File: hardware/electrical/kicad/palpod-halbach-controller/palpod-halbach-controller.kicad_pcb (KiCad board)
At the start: 4 copper layers, 150 x 100 mm, 0 parts

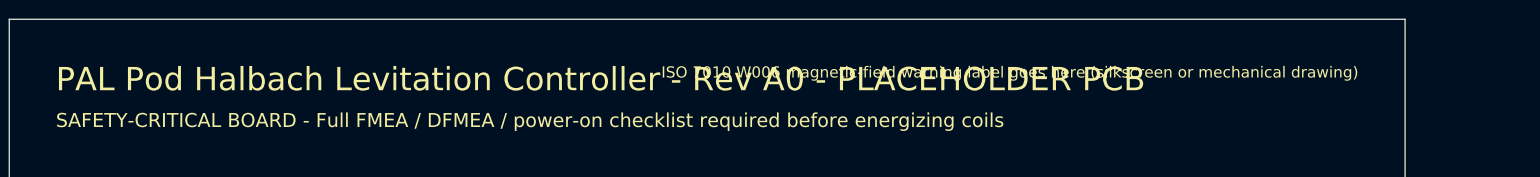
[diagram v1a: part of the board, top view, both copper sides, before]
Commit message: brand: broad KiCad sweep — remaining PAL Pod strings → Hearth
Targeted-pattern sed in ff14a48 missed variants. Broad find-replace
on .kicad_sch/pcb/pro/sym/mod + fp-lib-table + sym-lib-table +
per-project README.md (only where PAL Pod string actually appeared).
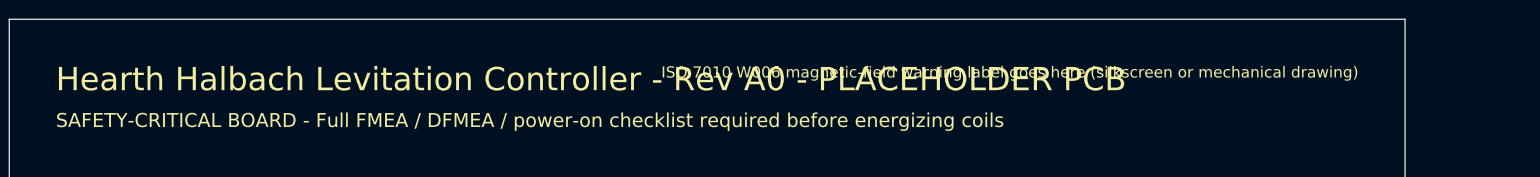
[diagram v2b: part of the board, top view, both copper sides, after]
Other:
- board text added: "Hearth Halbach Levitation Controller - Rev A0 - PLACEHOLDER PCB"
- board text removed: "PAL Pod Halbach Levitation Controller - Rev A0 - PLACEHOLDER PCB"
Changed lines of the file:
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@@
   (paper "A3")
   (title_block
-    (title "PAL Pod Halbach Levitation Controller - PCB")
+    (title "Hearth Halbach Levitation Controller - PCB")
     (date "2026-08-03")
     (rev "A0")
@@
     (layer "Edge.Cuts")
   )
-  (gr_text "PAL Pod Halbach Levitation Controller - Rev A0 - PLACEHOLDER PCB"
+  (gr_text "Hearth Halbach Levitation Controller - Rev A0 - PLACEHOLDER PCB"
     (at 55 55 0)
     (layer "F.SilkS")
